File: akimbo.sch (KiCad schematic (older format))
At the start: 73 parts, among them J1 USB mini-B, J2 3.5mm TRRS, J3 3.5mm TRRS, K1 -, K11 -, K12 -, K13 -, K14 -, K15 -, K16 -, K17 -, K18 -, K19 -, K2 -, K20 -, K21 -, K22 -, K23 -, K24 -, K25 -, K26 -, K27 -, K28 -, K29 -, K3 -, K30 -, K4 -, K6 -, K7 -, K8 -, K9 -, U1 ATmega32U4, U2 MCP23017_SO, Y1 16M

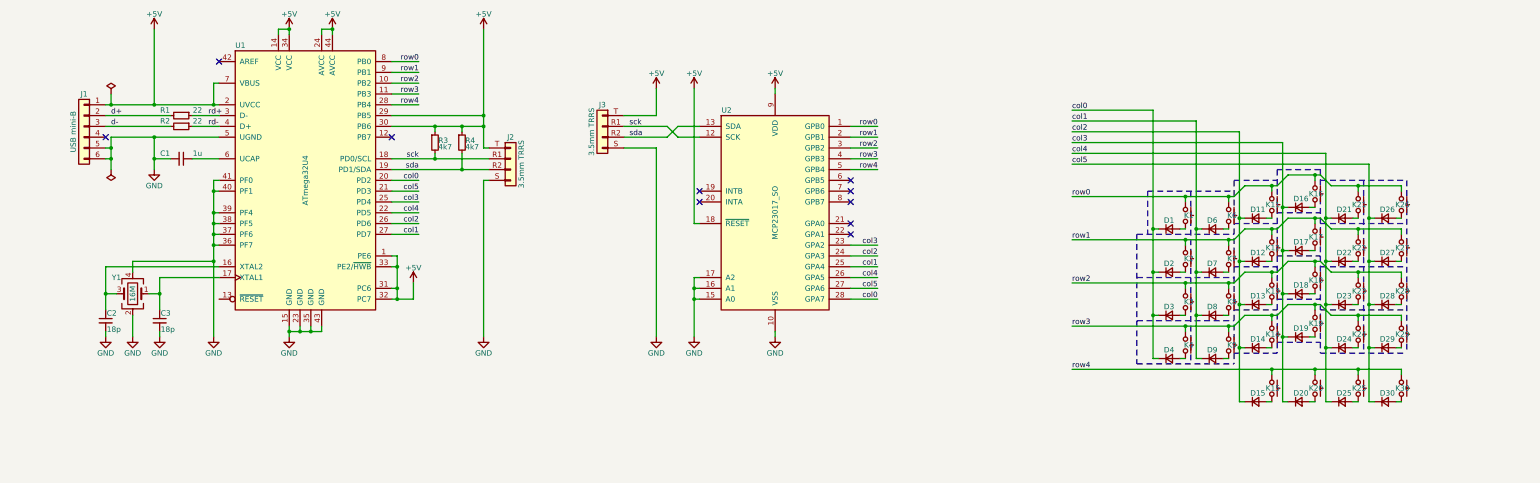
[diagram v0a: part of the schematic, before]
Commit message: USB-C instead of mini-B
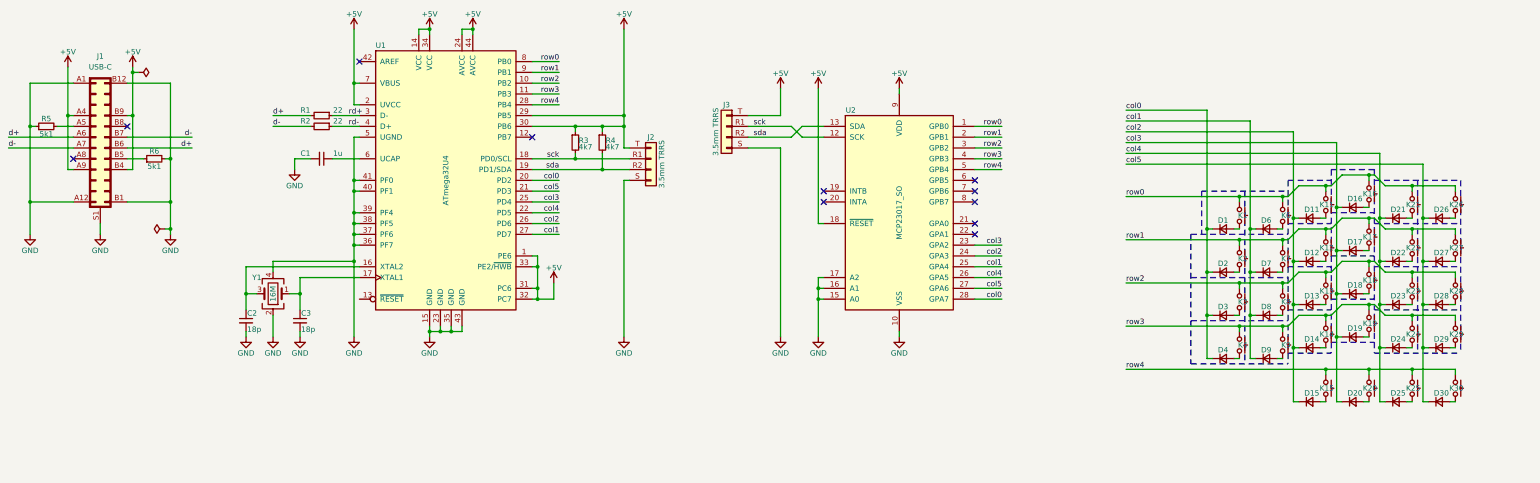
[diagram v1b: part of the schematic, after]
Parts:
- removed J1: USB mini-B, Connector_USB:USB_Mini-B_Lumberg_2486_01_Horizontal, symbol Connector_Generic:Conn_01x06
- added J1: USB-C, Connector_USB:USB_C_Receptacle_GCT_USB4085, symbol rk:Conn_USB-C_NoSS
- added R5, R6: 5k1, Resistor_SMD:R_0805_2012Metric_Pad1.15x1.40mm_HandSolder, symbol Device:R_Small
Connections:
- net +5V: now also J1.A4, J1.A9, J1.B4, J1.B9
- net GND: now also J1.A1, J1.A12, J1.B1, J1.B12, J1.S1 (Shield), R5.1, R6.2
- net d+: now also J1.A6, J1.B6
- net d-: now also J1.A7, J1.B7
- new net: J1.A5, R5.2
- new net: J1.B5, R6.1
- no-connect marks 10 -> 11
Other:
- moved on the sheet: C1, C2, C3, D1, D11, D12, D13, D14, D15, D16, D17, D18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
